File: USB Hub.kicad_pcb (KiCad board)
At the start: 4 copper layers, 60 x 95 mm, 92 parts, among them J1 Barrel_Jack_MountingPin, J2 10118193-0001LF, J3 10067847-001RLF, J4 UE27AC5410H, J5 UE27AC5410H, J6 UE27AC5410H, U1 TPS2116DRLR, U10 MIC2005A-1YM5-TR, U11 MIC2005A-1YM5-TR, U12 MIC2005A-1YM5-TR, U13 D1213A-04V-7, U14 D1213A-04V-7, U15 USBLC6-2SC6, U16 USBLC6-2SC6, U17 USBLC6-2SC6, U2 USBLC6-2SC6, U3 M24C02-WMN, U4 MIC5504-3.3YM5, U5 74LVC1G86, U6 74LVC1G04, U7 USB2514B_Bi, U8 MIC2005A-1YM5-TR, U9 GL823K-HCY04, Y1 ECS-240

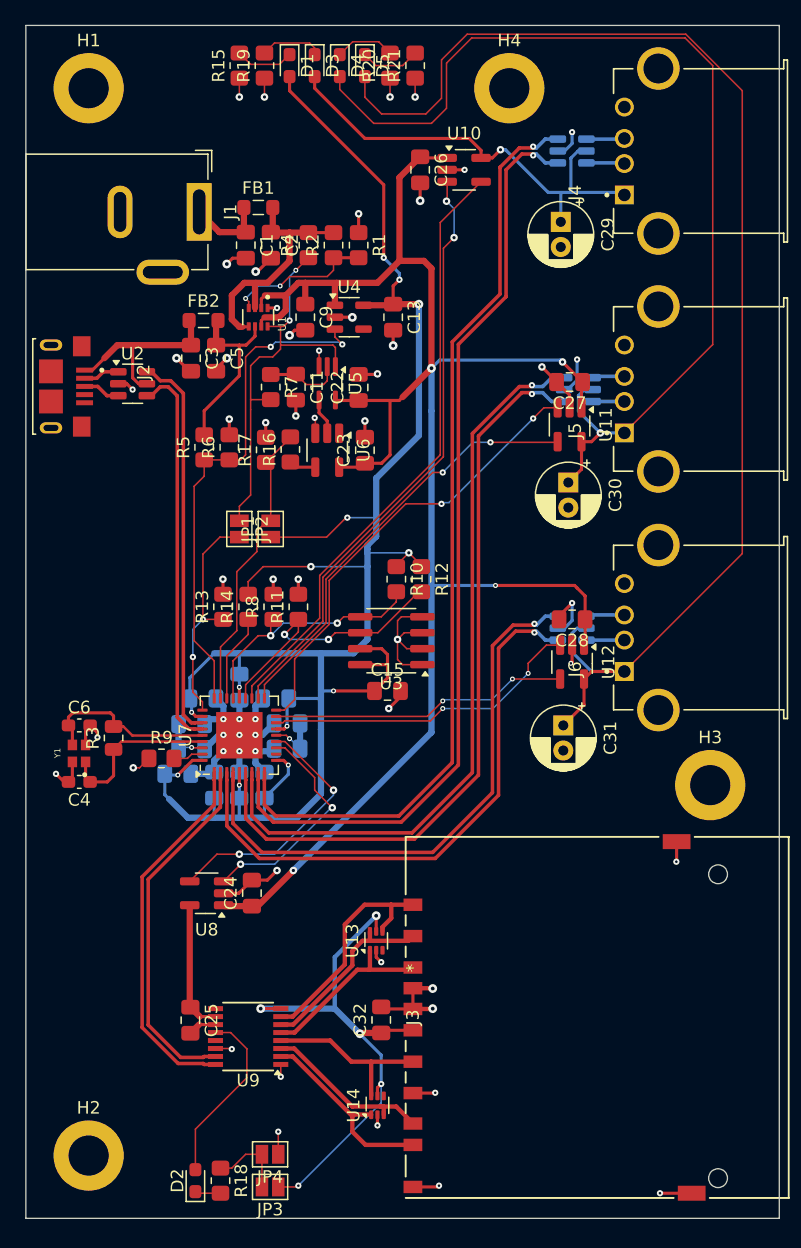
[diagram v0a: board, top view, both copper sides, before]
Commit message: Fixed reference designator silkscreen and add copper pours to power section
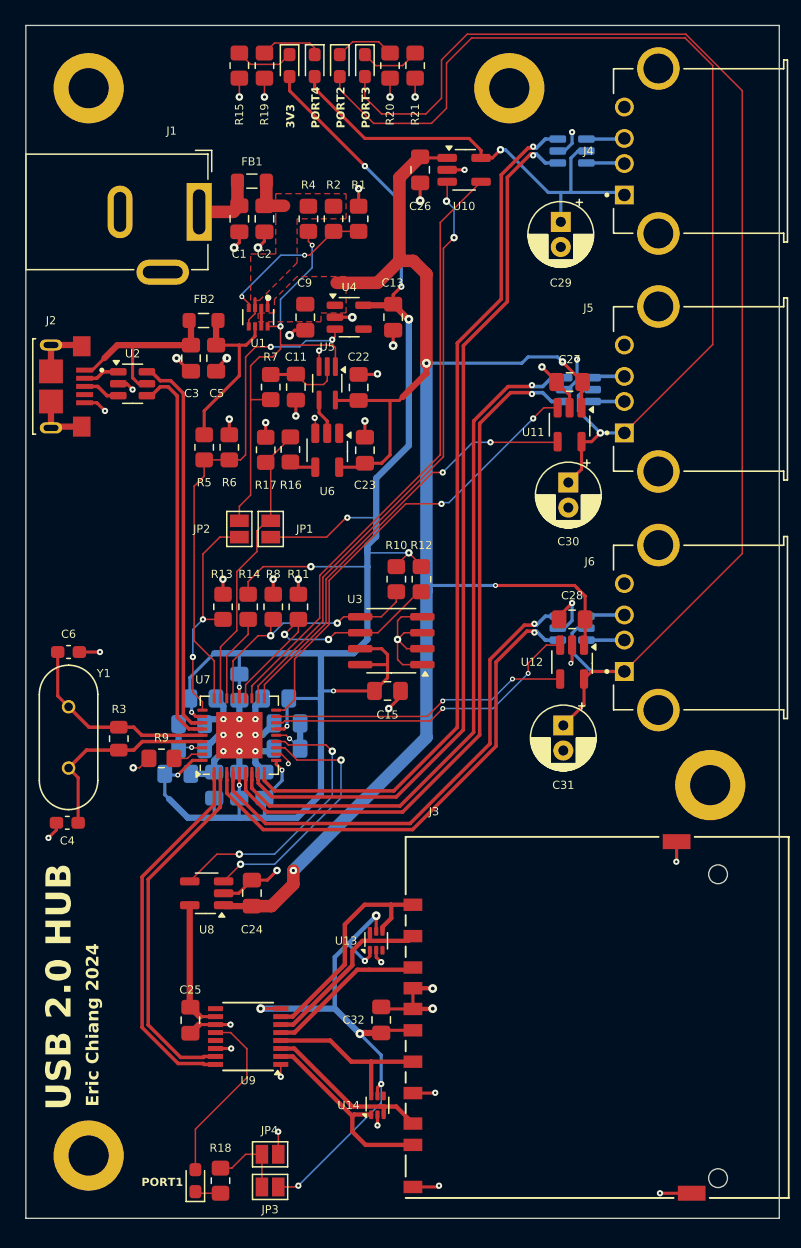
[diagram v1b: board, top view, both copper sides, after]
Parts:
- C4, C6: value 16p -> 8p
- Y1: value ECS-240 -> Crystal; footprint Custom Footprints:XTAL_ECS-240-12-37B-CKY-TR -> Custom Footprints:XTAL_HC49P488W43L1150T466H350
- moved C6 5.91 mm to (26.9, -62.6)
- moved C4 3.39 mm to (26.8, -49.0)
- moved C1 2.16 mm to (40.5, -97.1)
- moved C2 2.16 mm to (42.5, -97.1)
- moved FB1 2.16 mm to (41.5, -100.1)
- moved R1 2.10 mm to (50.0, -97.1)
- moved R2 2.10 mm to (48.0, -97.1)
- moved R4 2.10 mm to (46.0, -97.1)
- moved Y1 1.52 mm to (26.9, -55.8)
- moved R3 0.42 mm to (30.9, -55.7)
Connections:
- Y1 pad 2: GND -> Net-(U7-XTALOUT)
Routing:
- net 5V_FILTER: track 20.6 -> 6.01 mm
- net 5V: track 142.9 -> 130.6 mm
- net GND: track 121.9 -> 132.5 mm, vias 57 -> 60
- net /USB2_D-: track 46.4 -> 40.1 mm
- net /USB2_D+: track 45.6 -> 39.3 mm
- net /USB4_D-: track 75.1 -> 70.5 mm
- net /USB4_D+: track 74.3 -> 69.7 mm
- net /USB3_D-: track 60.7 -> 56.3 mm
- net /USB3_D+: track 59.8 -> 55.5 mm
- net 3V3_SD: track 43.0 -> 45.9 mm, vias 5 -> 6
- net Net-(U7-XTALIN/CLKIN): track 13.2 -> 16.1 mm
- net /USB1_EN: track 18.1 -> 20.7 mm
- net 3V3: track 164.0 -> 161.5 mm
- net /LOCAL_PWR: track 32.6 -> 34.8 mm
- net Net-(U7-XTALOUT): track 14.4 -> 16.4 mm
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- added copper zone on F.Cu, net 5V
- added copper zone on F.Cu, net 5V_FILTER
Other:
- board text added: "3V3"
- board text added: "Eric Chiang 2024"
- board text added: "PORT1"
- board text added: "PORT2"
- board text added: "PORT3"
- board text added: "PORT4"
- board text added: "USB 2.0 HUB"

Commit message: Fixed via stitching and sizes
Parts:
- moved C1 177.0 mm to (123.6, 59.2)
- moved C10 177.0 mm to (127.4, 99.4)
- moved C11 177.0 mm to (128.1, 72.6)
- moved C12 177.0 mm to (127.4, 101.4)
- moved C13 177.0 mm to (135.8, 67.0)
- moved C14 177.0 mm to (121.6, 104.3)
- moved C15 177.0 mm to (135.4, 96.8)
- moved C16 177.0 mm to (125.6, 104.3)
- moved C17 177.0 mm to (123.6, 104.3)
- moved C18 177.0 mm to (126.5, 97.4)
- moved C19 177.0 mm to (123.6, 96.5)
- moved C2 177.0 mm to (125.6, 59.2)
- moved C20 177.0 mm to (120.7, 97.4)
- moved C21 177.0 mm to (118.7, 103.4)
- moved C22 177.0 mm to (133.1, 72.6)
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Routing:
- net Net-(JP2-B): track 18.1 -> 22.4 mm
- net /EEPROM_SDA: track 22.3 -> 23.7 mm
- net /LOCAL_PWR: track 34.8 -> 35.8 mm
- net /USB3_OC: track 34.5 -> 35.5 mm
- net Net-(U1-PR1): track 12.7 -> 13.6 mm
- net GND: vias 60 -> 167

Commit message: v2 of USB Hub
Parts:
- removed the C11 at (128.1, 72.6)
- removed the C22 at (133.1, 72.6)
- removed the JP1 at (126.1, 83.9)
- removed JP3, JP4: ~, Jumper:SolderJumper-2_P1.3mm_Open_Pad1.0x1.5mm
- removed the R16 at (127.7, 77.6)
- removed the R17 at (125.7, 77.6)
- removed the R7 at (126.1, 72.6)
- removed the U5 at (130.6, 72.3)
- removed the U6 at (130.6, 77.6)
- added C24: 2u2, Capacitor_SMD:C_0805_2012Metric_Pad1.18x1.45mm_HandSolder, B.Cu at (115.0, 124.3)
- added C28: 100n, Capacitor_SMD:C_0805_2012Metric_Pad1.18x1.45mm_HandSolder, B.Cu at (115.0, 122.3)
- added JP2: SolderJumper_3_Open, Jumper:SolderJumper-3_P2.0mm_Open_TrianglePad1.0x1.5mm_NumberLabels, F.Cu at (124.0, 118.3)
- added R15: 10k, Resistor_SMD:R_0805_2012Metric_Pad1.20x1.40mm_HandSolder, F.Cu at (128.1, 78.9)
- added R5: 100k, Resistor_SMD:R_0805_2012Metric_Pad1.20x1.40mm_HandSolder, F.Cu at (136.2, 58.1)
- added SW1: 1825910-6, Library:SW4_1825910-B_TEC, F.Cu at (133.6, 76.8)
- added TP1: GND, TestPoint:TestPoint_THTPad_D4.0mm_Drill2.0mm, F.Cu at (109.5, 81.7)
- added TP2: SDA, TestPoint:TestPoint_THTPad_2.0x2.0mm_Drill1.0mm, F.Cu at (130.8, 82.1)
- added TP3: SCL, TestPoint:TestPoint_THTPad_2.0x2.0mm_Drill1.0mm, F.Cu at (128.2, 82.1)
- added TP4: 3V3_SD, TestPoint:TestPoint_THTPad_2.0x2.0mm_Drill1.0mm, F.Cu at (115.5, 128.4)
- C23: value 100n -> 4u7
- C29, C30, C31: value 100u -> 120uF
- R11, R13, R14, R8: moved to B.Cu
- U5: renamed from U7; footprint Package_DFN_QFN:QFN-36-1EP_6x6mm_P0.5mm_EP3.7x3.7mm -> Library:QFN-36-1EP_6x6mm_P0.5mm_EP3.7x3.7mm_ThermalVias
- moved C23 42.7 mm to (120.7, 118.3), turned to 0 degrees
- moved JP1 16.7 mm to (136.2, 73.0)
- moved C5 13.7 mm to (124.5, 88.5), turned to 180 degrees
- moved R12 13.7 mm to (124.5, 86.5), turned to 0 degrees
- moved R10 12.1 mm to (124.5, 84.5), turned to 0 degrees
- moved U3 8.23 mm to (130.4, 86.5)
- moved C25 6.56 mm to (142.0, 60.5), turned to 0 degrees
- moved R4 5.27 mm to (134.2, 58.1)
- moved R17 3.90 mm to (118.2, 135.7)
- moved U7 3.05 mm to (121.2, 124.2)
- moved C22 2.90 mm to (120.7, 120.3), turned to 0 degrees
- moved R6 2.76 mm to (122.8, 75.5)
- moved R7 2.65 mm to (120.9, 75.5)
- moved R13 1.81 mm to (120.7, 90.8)
- moved R14 1.81 mm to (122.7, 90.8)
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- renumbered C9 to C10, C10 to C11, C16 to C15, C17 to C16, C18 to C17, C19 to C18, C20 to C19, C21 to C20, C24 to C21, C25 to C22, C26 to C25, C27 to C26, C28 to C27, C15 to C5, C5 to C6, C6 to C7, C7 to C8, C8 to C9, J4 to J3, J5 to J4, J6 to J5, J3 to J6, JP2 to JP1, R15 to R16, R18 to R17, R19 to R18, R20 to R19, R21 to R20, R5 to R6, R6 to R7, U12 to U10, U13 to U11, U14 to U12, U15 to U13, U16 to U14, U17 to U15, U8 to U6, U9 to U7, U10 to U8, U11 to U9
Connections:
- C22 pad 1: Net-(U8-VOUT) -> Net-(U6-VOUT)
- C23 pad 1: 5V -> Net-(U6-VOUT)
- C32 pad 1: 3V3_SD -> 3V3_PMOS
- J6 pad 10: GND -> unconnected-(J6-CD-Pad10)
- J6 pad 4: 3V3_SD -> 3V3_PMOS
- R10 pad 2: /EEPROM_SCL -> /EEPROM_SDA
- R12 pad 2: /EEPROM_SDA -> /EEPROM_SCL
- R17 pad 1: Net-(JP3-B) -> 3V3_SD
- R17 pad 2: Net-(D2-K) -> Net-(D2-A)
- U1 pad 8: /LOCAL_PWR -> Net-(U1-ST)
- U11 pad 1: 3V3_SD -> 3V3_PMOS
- U11 pad 5: 3V3_SD -> 3V3_PMOS
- U12 pad 5: 3V3_SD -> 3V3_PMOS
- U3 pad 5: /EEPROM_SCL -> /EEPROM_SDA
- U3 pad 6: /EEPROM_SDA -> /EEPROM_SCL
- U6 pad 5: Net-(U8-VOUT) -> Net-(U6-VOUT)
- U7 pad 10: Net-(U8-VOUT) -> Net-(U6-VOUT)
- U7 pad 12: Net-(D2-A) -> Net-(D2-K)
- U7 pad 13: unconnected-(U9-VDDA-Pad13) -> 3V3_SD
- U7 pad 8: 3V3_SD -> Net-(JP2-A)
- U7 pad 9: unconnected-(U9-VDD-Pad9) -> 3V3_SD
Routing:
- net 3V3_PMOS: track 0.00 -> 33.0 mm, vias 0 -> 5
- net 3V3_SD: track 45.9 -> 21.0 mm, vias 6 -> 1
- net 5V: track 130.6 -> 108.9 mm
- net /LOCAL_PWR: track 35.8 -> 16.8 mm
- net Net-(JP1-B): track 22.4 -> 40.5 mm
- net Net-(U1-ST): track 0.00 -> 17.3 mm, vias 0 -> 2
- net /EEPROM_SCL: track 20.7 -> 37.8 mm, vias 2 -> 1
- net Net-(D2-A): track 14.4 -> 1.91 mm
- net GND: track 132.5 -> 120.7 mm, vias 167 -> 117
- net /USB4_OC: track 48.7 -> 59.7 mm, vias 0 -> 2
- net Net-(D2-K): track 2.05 -> 12.9 mm
- net Net-(U8-VOUT): track 10.5 -> 0.00 mm
- net 5V_FILTER: track 6.01 -> 16.4 mm
- net /RESET: track 23.6 -> 33.6 mm
- net Net-(U6-VOUT): track 0.00 -> 9.72 mm
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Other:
- board text added: "3V3 SD"
- board text added: "GND"
- board text added: "PORT 2"
- board text added: "PORT 3"
- board text added: "PORT 4"
- board text added: "RESET"
- board text added: "SCL"
- board text added: "SDA"
- board text added: "USB 2.0 HUB v2"
- board text removed: "USB 2.0 HUB"
